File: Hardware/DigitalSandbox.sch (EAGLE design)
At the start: 76 parts, among them Q1 MOSFET-N, Q2 MOSFET-P, U1 MCP73831, U2 ATMEGA328, U3 MCP9700, U4 FT232RLSSOP, U5 C2031N-1A2-B10K-GP, U6 TEMT6000, U7 V_REG_LDOSMD, U8 LMV358, U9 MIC9.7MM, X1 USB-SMD-NS, Y1 8MHz

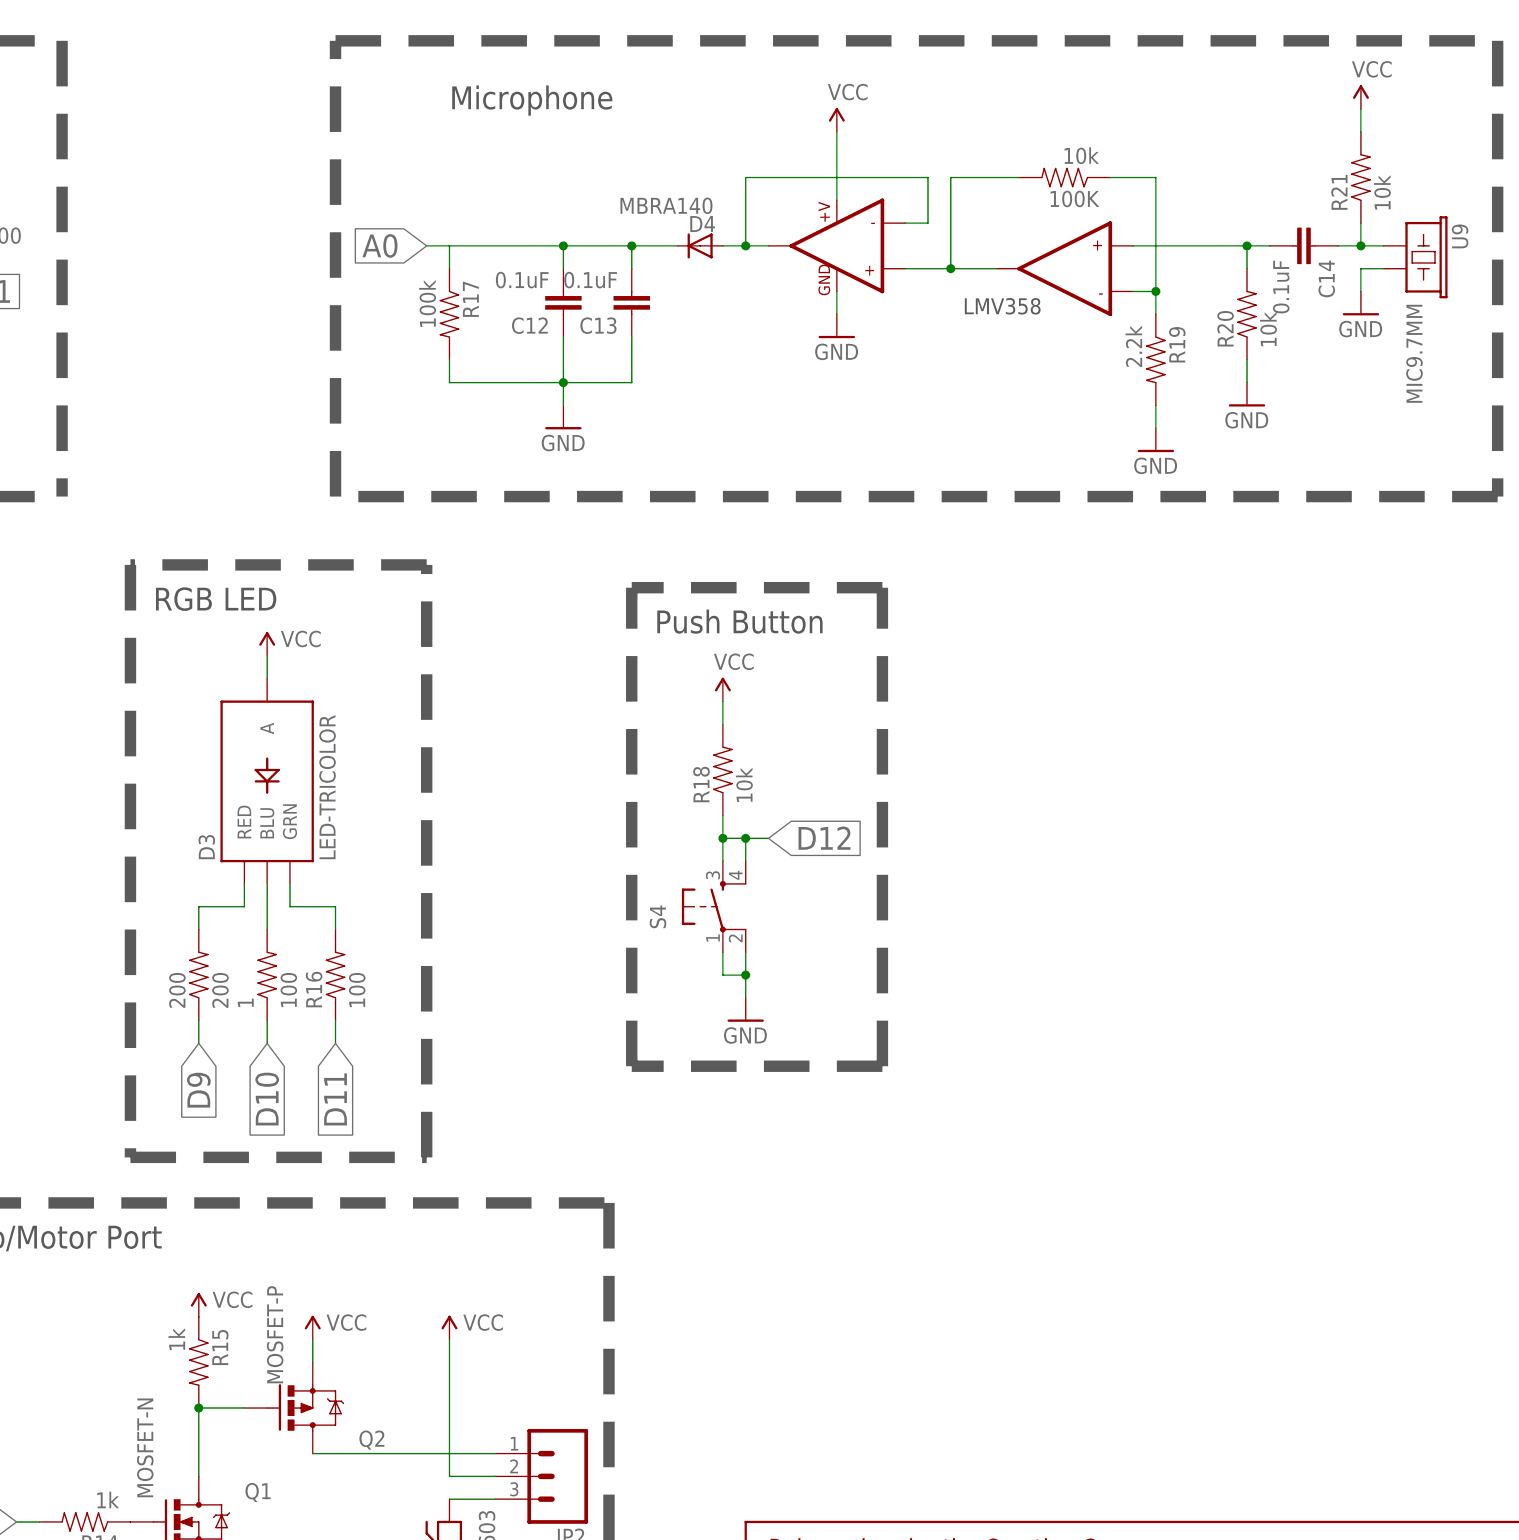
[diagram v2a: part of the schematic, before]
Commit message: fixed numbering issues with resistors
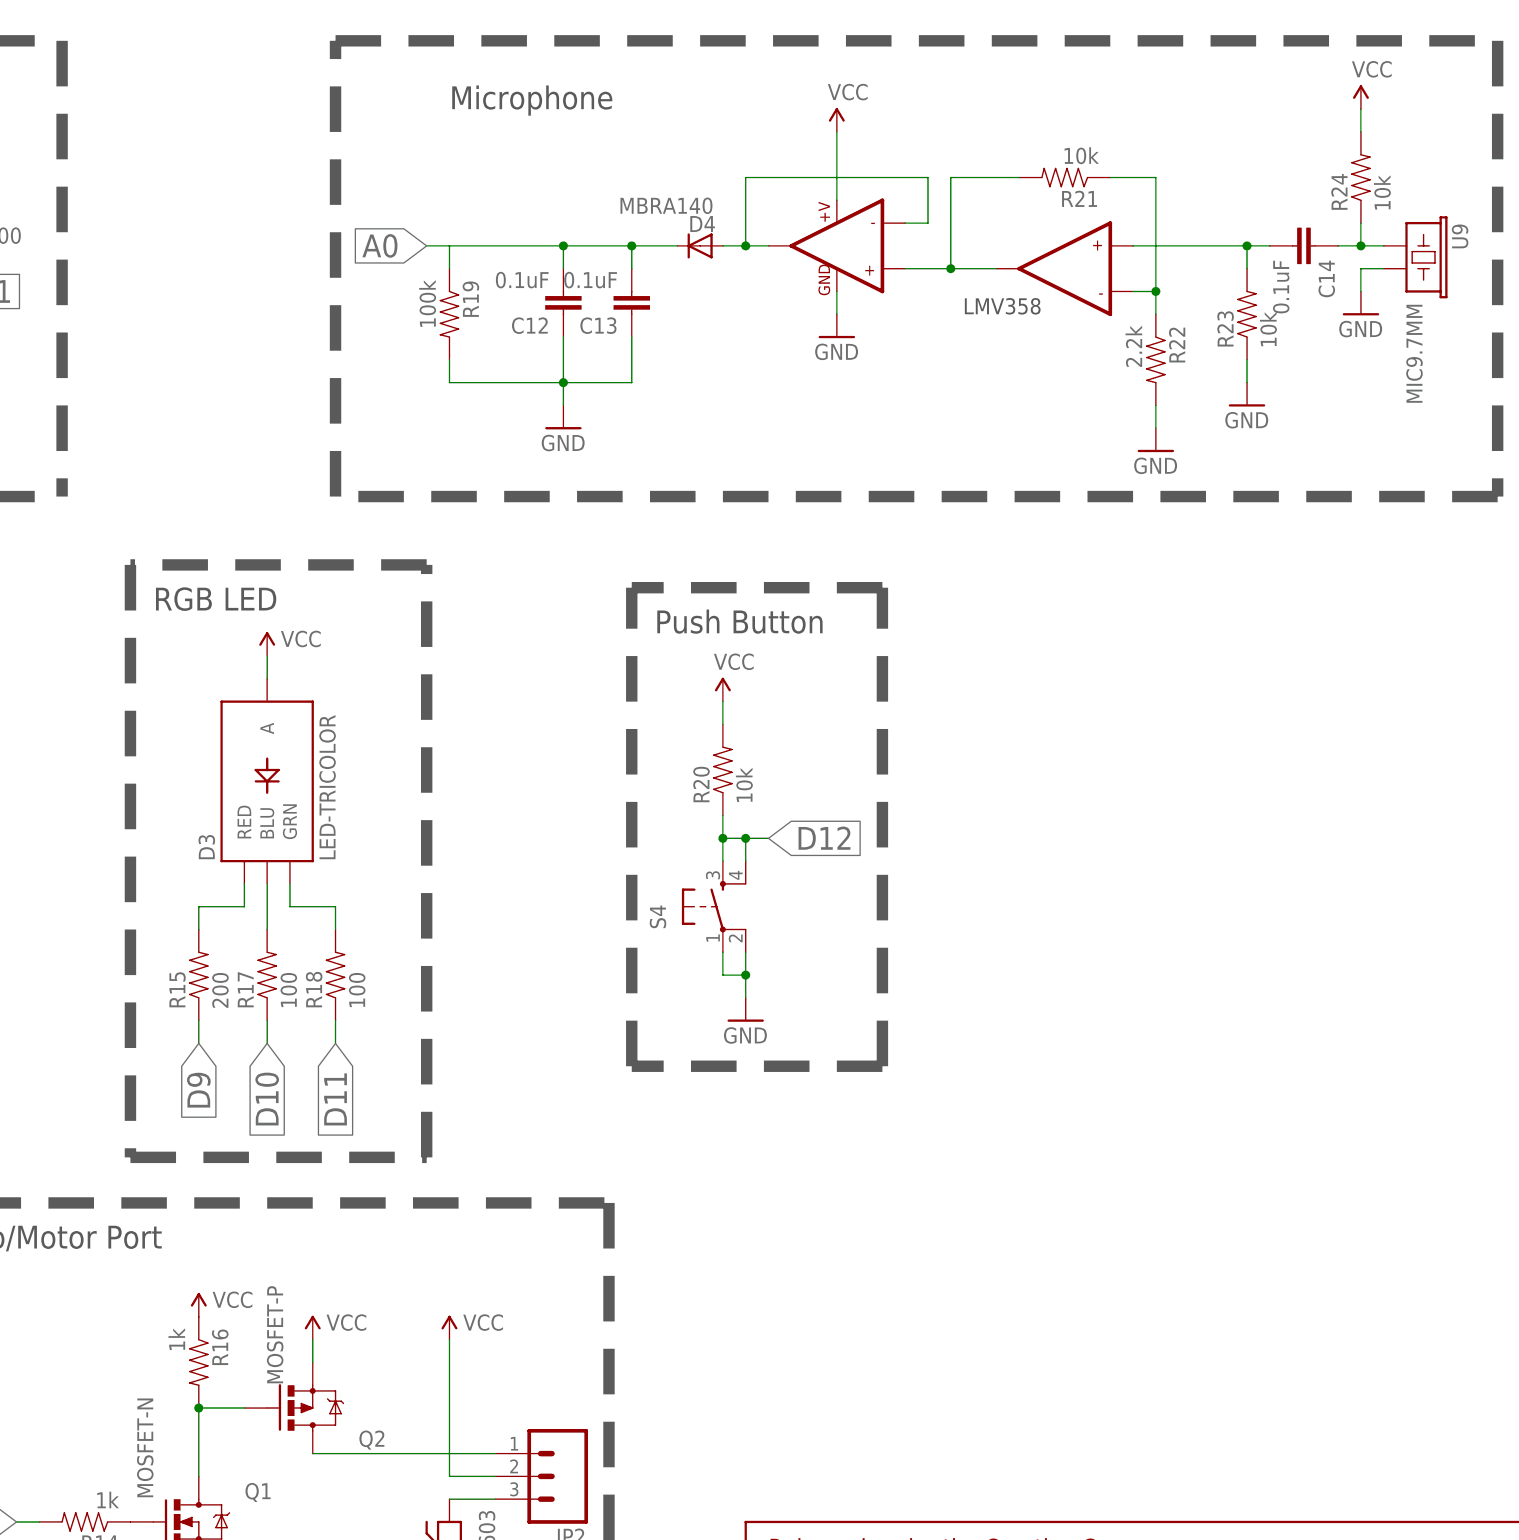
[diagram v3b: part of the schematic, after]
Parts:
- removed 1: 100, SparkFun-Passives:RESISTOR0603-RES
- removed 100K: 10k, SparkFun-Passives:RESISTOR0603-RES
- removed 200: 200, SparkFun-Passives:RESISTOR0603-RES
- added R22: 2.2k, SparkFun-Passives:RESISTOR0603-RES
- added R23, R24: 10k, SparkFun-Passives:RESISTOR0603-RES
- C10, C7: device SparkFun:CAP0402-CAP -> SparkFun:CAP0603-CAP
- R15: value 1k -> 200
- R16: value 100 -> 1k
- R17: value 100k -> 100
- R18: value 10k -> 100
- R19: value 2.2k -> 100k
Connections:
- net A0: now also R19.1; no longer R17.1
- net BLU: now also R17.2; no longer 1.2
- net D10: now also R17.1; no longer 1.1
- net D11: now also R18.1; no longer R16.1
- net D12: now also R20.1; no longer R18.1
- net D9: now also R15.1; no longer 200.1
- net GND: now also R22.2, R23.1; no longer R17.2, R20.1
- net GRN: now also R18.2; no longer R16.2
- net N$17: now also R24.1; no longer R21.1
- net N$20: now also R23.2; no longer R20.2
- net N$23: now also R21.1, R22.1; no longer 100K.1, R19.1
- net N$26: now also R21.2; no longer 100K.2
- net N$4: now also R16.2; no longer R15.2
- net RED: now also R15.2; no longer 200.2
- net VCC: now also R16.1, R20.2, R24.2; no longer R15.1, R18.2, R21.2
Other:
- moved on the sheet: R15, R16, R17, R18, R19, R20, R21

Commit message: Added Mosfets and updated numbering
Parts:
- added Q3, Q4, Q5: MOSFET-N, SparkFun-DiscreteSemi:MOSFET-NCHANNELBSS138
- added R25: 2.2k, SparkFun-Passives:RESISTOR0603-RES
- added R26, R27: 10k, SparkFun-Passives:RESISTOR0603-RES
- F1, F2: value PTC0603 -> PTCSMD; device SparkFun-PowerIC:PTC0603 -> SparkFun-PowerIC:PTCSMD
- LED1, LED2, LED3, LED4, LED5: value (none) -> White
- R11: value 1k -> 100
- R12, R21: value 10k -> 100
- R14: value 1k -> 10k
- R15: value 200 -> 1k
- R17: value 100 -> 200
- R18, R6, R7: value 100 -> 1k
- R19: value 100k -> 100
- R20: value 10k -> 1k
- R22: value 2.2k -> 100k
- R4: value 330 -> 10k
- R5: value 10k -> 330
- S2: value On/Off -> AYZ0202
- S3: value AYZ0202 -> On/Off
- U3: value MCP9700 -> C2031N-1A2-B10K-GP; device SparkFun:MCP9700SMD -> C2031N-1A2-B10K-GP:C2031N-1A2-B10K-GP
- U4: value FT232RLSSOP -> MCP9700; device SparkFun:FT232RLSSOP -> SparkFun:MCP9700SMD
- U5: value C2031N-1A2-B10K-GP -> FT232RLSSOP; device C2031N-1A2-B10K-GP:C2031N-1A2-B10K-GP -> SparkFun:FT232RLSSOP
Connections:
- removed net BLU: D3.BLU, R17.2
- new net N$14: Q3.G, R16.2
- new net N$19: Q4.G, R18.2
- new net N$22: Q5.G, R20.1
- new net N$25: Q5.D, R21.1
- new net N$27: Q4.D, R19.1
- new net N$28: D3.BLU, R19.2
- new net N$29: Q3.D, R17.1
- net 3.3V: now also U5.3V3OUT; no longer U4.3V3OUT
- net 5V: now also R15.2, S3.1, S3.4, U5.VCC, U5.VCCIO; no longer R11.2, S2.1, S2.4, U4.VCC, U4.VCCIO
- net A0: now also R22.1; no longer R19.1
- net A1: now also R14.1; no longer R12.1
- net A2: now also U4.VO; no longer U3.VO
- net A3: now also U3.S; no longer U5.S
- net CTS: now also U5.CTS; no longer U4.CTS
- net D10: now also R18.1; no longer R17.1
- net D11: now also R20.2; no longer R18.1
- net D12: now also R23.1; no longer R20.1
- net D13: now also R5.2; no longer R4.2
- net D2: now also R3.2; no longer R5.2
- net D3: now also R6.2; no longer R14.2
- net D9: now also R16.1; no longer R15.1
- net DTR: now also U5.DTR; no longer U4.DTR
- net GND: now also F1.1, Q3.S, Q4.S, Q5.S, R11.2, R14.2, R25.2, R26.1, R4.1, S2.3, S2.6, U3.A, U4.GND, U5.AGND, U5.GND18, U5.GND21, U5.GND7, U5.TEST; no longer F2.1, R19.2, R23.1, R3.1, R6.2, R7.2, S3.3, S3.6, U3.GND, U4.AGND, U4.GND18, U4.GND21, U4.GND7, U4.TEST, U5.A
- net GRN: now also R21.2; no longer R18.2
- net N$10: now also R6.1; no longer R14.1
- net N$11: now also R11.1; no longer R9.1
- net N$13: now also R12.1; no longer R10.1
- net N$15: now also R3.1, S2.2, S2.5; no longer R5.1, S3.2, S3.5
- net N$16: now also F1.2; no longer F2.2
- net N$17: now also R27.1; no longer R24.1
- net N$18: now also R8.1; no longer R6.1
- net N$2: now also R5.1; no longer R4.1
- net N$20: now also R26.2; no longer R23.2
- net N$21: now also R9.1; no longer R7.1
- net N$23: now also R24.1, R25.1; no longer R21.1, R22.1
- net N$26: now also R24.2; no longer R21.2
- net N$4: now also R7.2; no longer R16.2
- net N$5: now also R13.1; no longer R11.1
- net N$6: now also R15.1; no longer R13.1
- net N$7: now also F2.1; no longer F1.2
- net N$9: now also R10.1; no longer R8.1
- net PROG: now also R4.2; no longer R3.2
- net RED: now also R17.2; no longer R15.2
- net RXI: now also U5.RXD; no longer U4.RXD
- net RXLED: now also U5.RXLED; no longer U4.RXLED
- net TXLED: now also U5.TXLED; no longer U4.TXLED
- net TXO: now also U5.TXD; no longer U4.TXD
- net USB_D+: now also U5.USBDP; no longer U4.USBDP
- net USB_D-: now also U5.USBDM; no longer U4.USBDM
- net VBATT: now also S3.3, S3.6; no longer S2.3, S2.6
- net VCC: now also F2.2, R23.2, R27.2, R7.1, S2.1, S2.4, S3.2, S3.5, U3.E, U4.VCC; no longer F1.1, R16.1, R20.2, R24.2, S2.2, S2.5, S3.1, S3.4, U3.VCC, U5.E
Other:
- moved on the sheet: D3, F1, F2, JP2, Q1, Q2, R10, R11, R12, R13, R14, R15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
